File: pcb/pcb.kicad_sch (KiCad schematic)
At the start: 7 parts

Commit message: WIP
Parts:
- removed C? (x2): 100n, Capacitor_SMD:C_0603_1608Metric, symbol Device:C
- removed C? (x2): 22u, Capacitor_SMD:CP_Elec_4x3.9, symbol Device:C_Polarized_Small
- removed J?: EURO_PWR_2x5, Connector_IDC:IDC-Header_2x05_P2.54mm_Vertical, symbol eurocad:EURO_PWR_2x5
- removed R? (x2): 22R, Resistor_SMD:R_0603_1608Metric, symbol Device:R
- added A1: Arduino_Nano_v3.x, Module:Arduino_Nano, symbol MCU_Module:Arduino_Nano_v3.x
- added C1: 10u, Capacitor_THT:CP_Radial_D5.0mm_P2.50mm, symbol Device:C_Polarized
- added D1: 1N4148, Diode_THT:D_DO-35_SOD27_P7.62mm_Horizontal, symbol Diode:1N4148
- added D2: LED, LED_THT:LED_D5.0mm, symbol Device:LED
- added J1, J2, J3: PJ301M-12, Eurocad:PJ301M-12, symbol eurocad:PJ301M-12
- added JP1: Jumper, TestPoint:TestPoint_2Pads_Pitch2.54mm_Drill0.8mm, symbol Jumper:Jumper_2_Open
- added JP2: Jumper, Jumper:SolderJumper-2_P1.3mm_Open_RoundedPad1.0x1.5mm, symbol Jumper:SolderJumper_2_Open
- added R1, R2, R5, R6: 1K, Resistor_THT:R_Axial_DIN0207_L6.3mm_D2.5mm_P7.62mm_Horizontal, symbol Device:R
- added R3: 10K, Resistor_THT:R_Axial_DIN0207_L6.3mm_D2.5mm_P7.62mm_Horizontal, symbol Device:R
- added R4: 220R, Resistor_THT:R_Axial_DIN0207_L6.3mm_D2.5mm_P7.62mm_Horizontal, symbol Device:R
- added RV1, RV2: B100K, Potentiometer_THT:Potentiometer_Alpha_RD901F-40-00D_Single_Vertical, symbol Device:R_Potentiometer
- added SW1, SW2, SW3, SW4, SW5, SW6, SW7, SW8: 12x12 Tactile, Button_Switch_THT:SW_PUSH-12mm, symbol Switch:SW_Push
- added U1: MCP4901, Package_DIP:DIP-8_W7.62mm, symbol Analog_DAC:MCP4901
- added U2: 6N137, Package_DIP:DIP-8_W7.62mm, symbol Isolator:6N137
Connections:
- net GND: now also A1.29 (GND), A1.4 (GND), J1.1, J2.1, JP2.2 (B), R2.1, R5.2, RV1.1, RV2.1, SW1.1, SW2.1, SW3.1, SW4.1, SW5.1, SW6.1, SW7.1, SW8.1, U1.5 (~{LDAC}), U1.7 (Vss), U2.5 (GND)
- new net: C1.1, R1.2
- new net: J1.2, JP1.2 (B)
- new net: C1.2, J1.3, JP1.1 (A)
- new net: D2.1 (K), R5.1
- new net: D2.2 (A), J2.3, R6.2
- new net: D1.1 (K), R4.1, U2.2 (A)
- new net: D1.2 (A), J3.2, U2.3 (C)
- new net: J3.1, JP2.1 (A)
- new net: J3.3, R4.2
- new net +5V: A1.27 (+5V), R3.2, RV1.3, RV2.3, U1.1 (Vdd), U1.6 (Vref), U2.7 (EN), U2.8 (VCC)
- new net CLOCK_OUT: A1.15 (D12), R6.1
- new net CS: A1.13 (D10), U1.2 (~{CS})
- new net OUT: R1.1, R2.2, U1.8 (Vout)
- new net POT_1: A1.19 (A0), RV1.2
- new net POT_2: A1.20 (A1), RV2.2
- new net RX: A1.2 (D0/RX), R3.1, U2.6 (VO)
- new net SCK: A1.16 (D13), U1.3 (SCK)
- new net SDI: A1.14 (D11), U1.4 (SDI)
- new net SW_1: A1.10 (D7), SW1.2
- new net SW_2: A1.7 (D4), SW2.2
- new net SW_3: A1.5 (D2), SW3.2
- new net SW_4: A1.24 (A5), SW4.2
- new net SW_5: A1.6 (D3), SW5.2
- new net SW_6: A1.11 (D8), SW6.2
- new net SW_7: A1.23 (A4), SW7.2
- new net SW_8: A1.22 (A3), SW8.2
- new net TX: A1.1 (D1/TX)
- no-connect marks 0 -> 4

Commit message: Revert MIDI jack
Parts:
- removed JP2: Jumper, Jumper:SolderJumper-2_P1.3mm_Open_RoundedPad1.0x1.5mm, symbol Jumper:SolderJumper_2_Open
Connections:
- net GND: now also J3.1
- net at D1.2 (A), U2.3 (C): now also J3.3; no longer J3.2
- net at R4.2: now also J3.2; no longer J3.3
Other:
- moved on the sheet: J3
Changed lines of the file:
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@@
 	(wire
 		(pts
-			(xy 182.88 138.43) (xy 196.85 138.43)
-		)
-		(stroke
-			(width 0)
-			(type default)
-		)
-	)
-	(wire
-		(pts
 			(xy 73.66 162.56) (xy 69.85 162.56)
 		)
@@
 	(wire
 		(pts
-			(xy 191.77 142.24) (xy 190.5 142.24)
+			(xy 43.18 77.47) (xy 41.91 77.47)
 		)
 		(stroke
@@
 	(wire
 		(pts
-			(xy 43.18 77.47) (xy 41.91 77.47)
+			(xy 182.88 138.43) (xy 196.85 138.43)
 		)
 		(stroke
@@
 	(wire
 		(pts
-			(xy 205.74 99.06) (xy 218.44 99.06)
+			(xy 182.88 132.08) (xy 190.5 132.08)
 		)
 		(stroke
@@
 	(wire
 		(pts
-			(xy 182.88 135.89) (xy 199.39 135.89)
+			(xy 205.74 99.06) (xy 218.44 99.06)
 		)
 		(stroke
@@
 	(wire
 		(pts
+			(xy 182.88 135.89) (xy 199.39 135.89)
+		)
+		(stroke
+			(width 0)
+			(type default)
+		)
+	)
+	(wire
+		(pts
 			(xy 30.48 92.71) (xy 31.75 92.71)
 		)
@@
 	)
 	(symbol
-		(lib_id "Jumper:SolderJumper_2_Open")
-		(at 186.69 142.24 0)
-		(unit 1)
-		(exclude_from_sim yes)
-		(in_bom no)
-		(on_board yes)
-		(dnp no)
-		(property "Reference" "JP2"
-			(at 186.69 140.208 0)
-			(effects
-				(font
-					(size 1.27 1.27)
-				)
-			)
-		)
-		(property "Value" "Jumper"
-			(at 186.69 144.272 0)
-			(effects
-				(font
-					(size 1.27 1.27)
-				)
-			)
-		)
-		(property "Footprint" "Jumper:SolderJumper-2_P1.3mm_Open_RoundedPad1.0x1.5mm"
-			(at 186.69 142.24 0)
-			(effects
-				(font
-					(size 1.27 1.27)
-				)
-				(hide yes)
-			)
-		)
-		(property "Datasheet" "~"
-			(at 186.69 142.24 0)
-			(effects
-				(font
-					(size 1.27 1.27)
-				)
-				(hide yes)
-			)
-		)
-		(property "Description" "Solder Jumper, 2-pole, open"
-			(at 186.69 142.24 0)
-			(effects
-				(font
-					(size 1.27 1.27)
-				)
-				(hide yes)
-			)
-		)
-		(pin "2"
-		)
-		(pin "1"
-		)
-		(instances
-			(project ""
-				(path "/e63e39d7-6ac0-4ffd-8aa3-1841a4541b55"
-					(reference "JP2")
-					(unit 1)
-				)
-			)
-		)
-	)
-	(symbol
 		(lib_id "Switch:SW_Push")
 		(at 36.83 107.95 0)
@@
 	(symbol
 		(lib_id "power:GND")
-		(at 191.77 142.24 0)
+		(at 190.5 132.08 0)
 		(unit 1)
 		(exclude_from_sim no)
@@
 		(on_board yes)
 		(dnp no)
-		(fields_autoplaced yes)
 		(property "Reference" "#PWR027"
-			(at 191.77 148.59 0)
+			(at 190.5 138.43 0)
 			(effects
 				(font
@@
 		)
 		(property "Value" "GND"
-			(at 191.77 147.32 0)
+			(at 190.5 137.16 0)
 			(effects
 				(font
@@
 		)
 		(property "Footprint" ""
-			(at 191.77 142.24 0)
+			(at 190.5 132.08 0)
 			(effects
 				(font
@@
 		)
 		(property "Datasheet" ""
-			(at 191.77 142.24 0)
+			(at 190.5 132.08 0)
 			(effects
 				(font
@@
 		)
 		(property "Description" "Power symbol creates a global label with name \"GND\" , ground"
-			(at 191.77 142.24 0)
+			(at 190.5 132.08 0)
 			(effects
 				(font
@@
 	(symbol
 		(lib_id "eurocad:PJ301M-12")
-		(at 171.45 138.43 0)
-		(mirror x)
+		(at 171.45 135.89 0)
 		(unit 1)
 		(exclude_from_sim no)
@@
 		(dnp no)
 		(property "Reference" "J3"
-			(at 169.545 148.59 0)
+			(at 169.545 125.73 0)
 			(effects
 				(font
@@
 		)
 		(property "Value" "PJ301M-12"
-			(at 169.545 146.05 0)
+			(at 169.545 128.27 0)
 			(effects
 				(font
@@
 		)
 		(property "Footprint" "Eurocad:PJ301M-12"
-			(at 171.45 138.43 0)
+			(at 171.45 135.89 0)
 			(effects
 				(font
@@
 		)
 		(property "Datasheet" ""
-			(at 171.45 138.43 0)
+			(at 171.45 135.89 0)
 			(effects
 				(font
@@
 		)
 		(property "Description" ""
-			(at 171.45 138.43 0)
+			(at 171.45 135.89 0)
 			(effects
 				(font

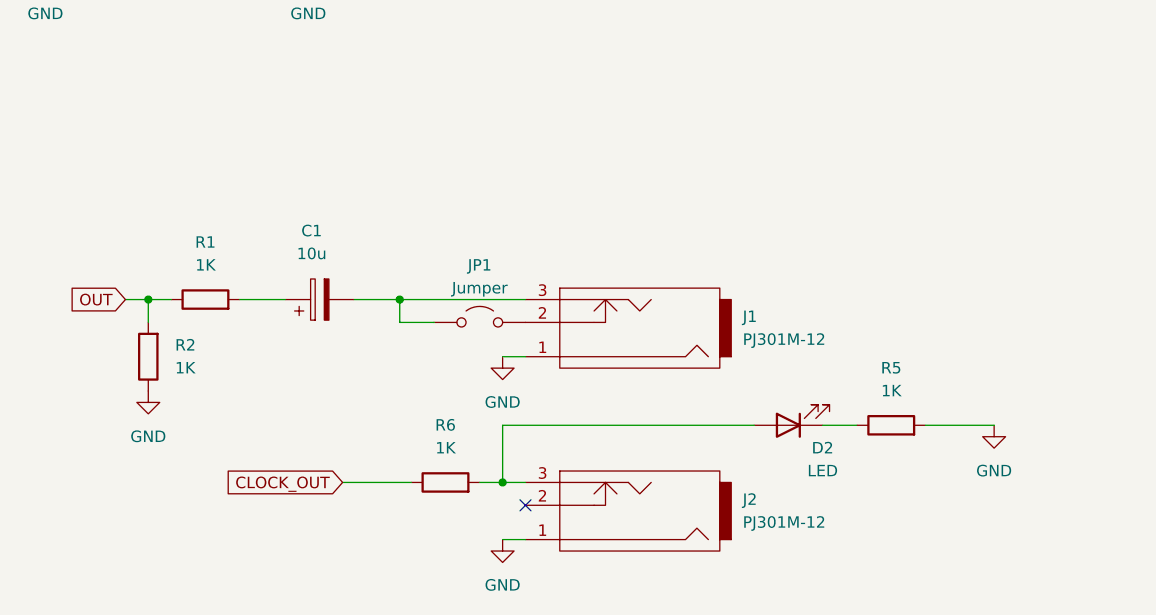
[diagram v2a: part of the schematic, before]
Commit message: Fix clock output
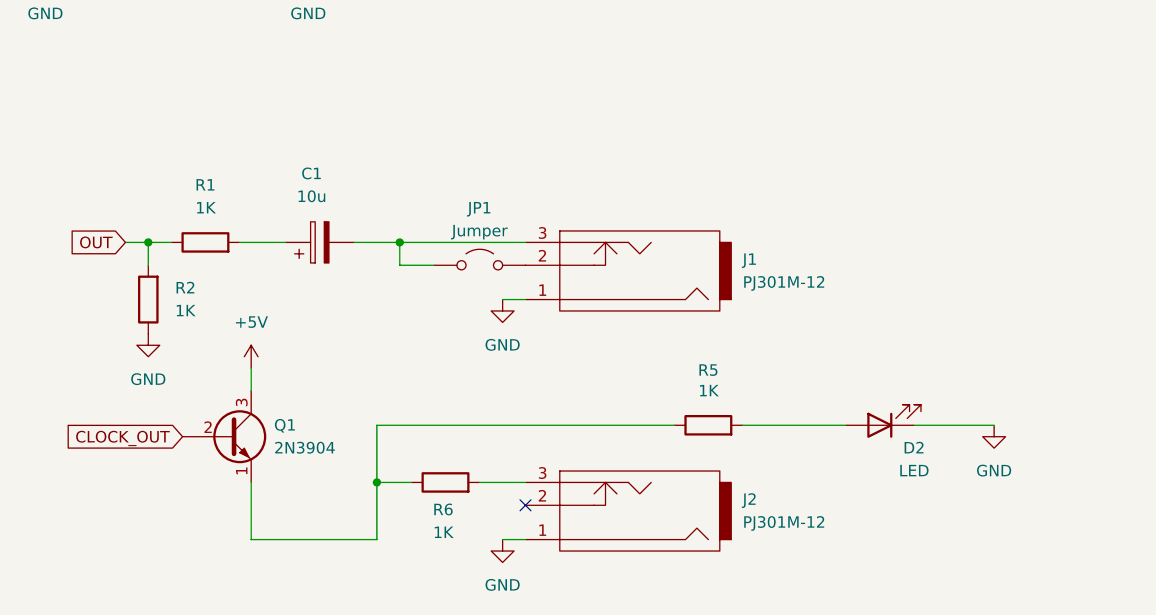
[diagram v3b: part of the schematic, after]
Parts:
- added Q1: 2N3904, Package_TO_SOT_THT:TO-92_Inline, symbol Transistor_BJT:2N3904
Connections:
- net +5V: now also Q1.3 (C)
- net CLOCK_OUT: now also Q1.2 (B); no longer R6.1
- net GND: now also D2.1 (K); no longer R5.2
- net at R5.1: now also R6.1, Q1.1 (E); no longer D2.1 (K)
- net at J2.3, R6.2: no longer D2.2 (A)
- new net: D2.2 (A), R5.2
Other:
- moved on the sheet: C1, D2, J1, JP1, R1, R2, R5
